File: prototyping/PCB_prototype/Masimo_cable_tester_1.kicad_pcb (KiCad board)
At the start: 2 copper layers, 70 x 80 mm, 30 parts, among them J1 Touchscreen HMI, J10 MCU Board Power, J16 Debug Connections, J17 Banana Jack, J2 Curiosity Nano AVR128DB48, J3 Conn_01x28_Socket, J4 Barrel Jack 9V, J5 MicroSD PinHeader, J6 SFML-110-02-L-D-A, J7 HMI Power Toggle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

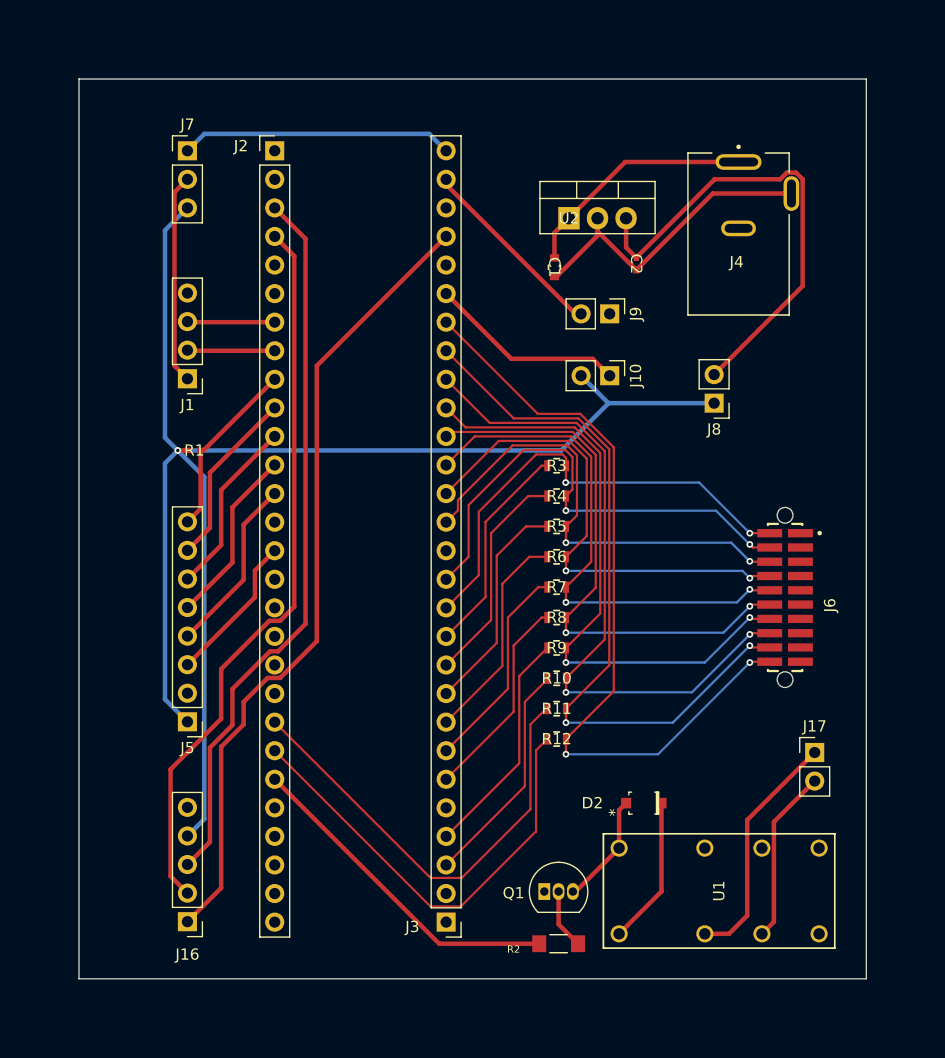
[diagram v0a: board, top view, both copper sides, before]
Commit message: Added ground plane.
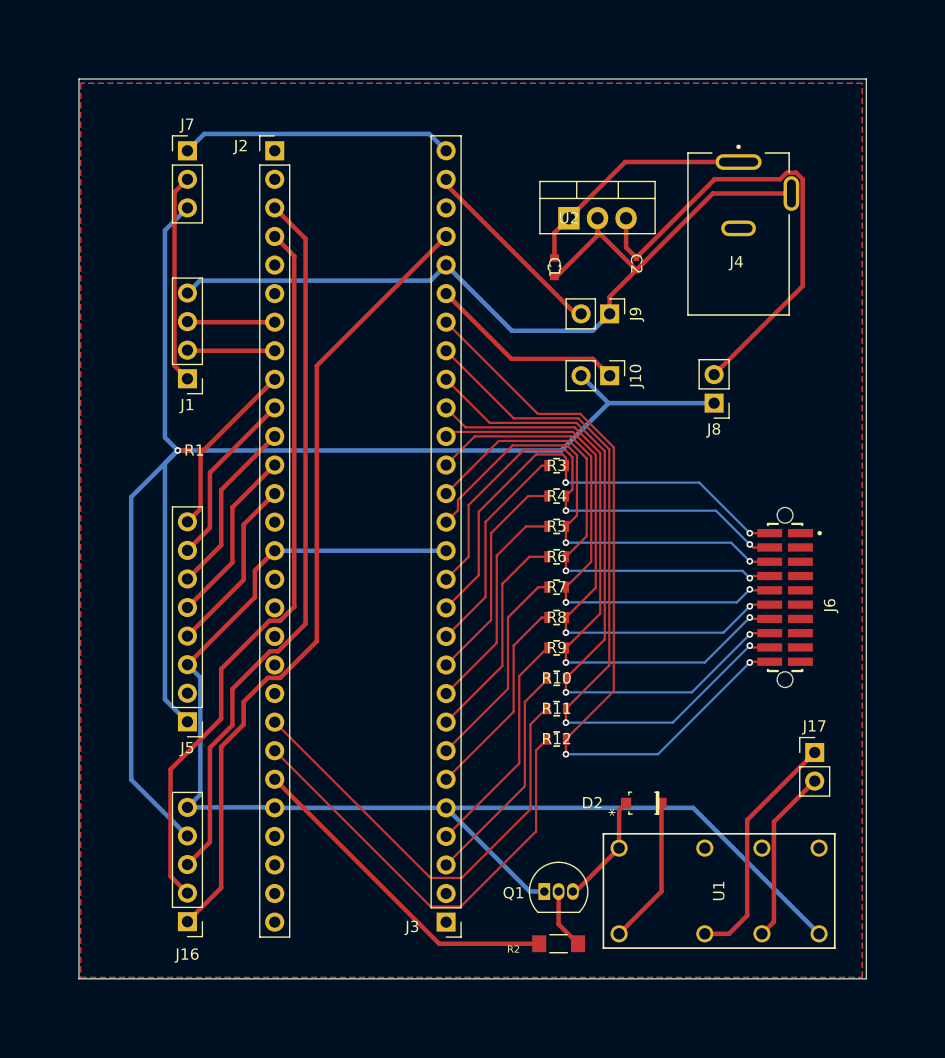
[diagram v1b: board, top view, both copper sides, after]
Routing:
- net GND: track 42.9 -> 190.9 mm
- net 5V: track 151.1 -> 153.3 mm
- added copper zone on B.Cu, net GND
- added copper zone on F.Cu, net GND
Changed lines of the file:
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@@
+	)
+	(segment
+		(start 127.54 70.975)
+		(end 129.9072 68.6078)
+		(width 0.4)
+		(layer "F.Cu")
+		(net 1)
 	)
 	(segment
@@
 		(width 0.4)
 		(layer "F.Cu")
+		(net 1)
+	)
+	(segment
+		(start 127.54 72.5)
+		(end 127.54 70.975)
+		(width 0.4)
+		(layer "F.Cu")
+		(net 1)
+	)
+	(segment
+		(start 118.84 74)
+		(end 126.04 74)
+		(width 0.4)
+		(layer "B.Cu")
+		(net 1)
+	)
+	(segment
+		(start 91.151 104.8411)
+		(end 91.151 115.229)
+		(width 0.4)
+		(layer "B.Cu")
+		(net 1)
+	)
+	(segment
+		(start 113 116.42)
+		(end 120.44 123.86)
+		(width 0.4)
+		(layer "B.Cu")
+		(net 1)
+	)
+	(segment
+		(start 113 68.16)
+		(end 111.611 69.549)
+		(width 0.4)
+		(layer "B.Cu")
+		(net 1)
+	)
+	(segment
+		(start 91.151 115.229)
+		(end 90 116.38)
+		(width 0.4)
+		(layer "B.Cu")
+		(net 1)
+	)
+	(segment
+		(start 134.96 116.42)
+		(end 146.16 127.62)
+		(width 0.4)
+		(layer "B.Cu")
+		(net 1)
+	)
+	(segment
+		(start 113 116.42)
+		(end 97.76 116.42)
+		(width 0.4)
+		(layer "B.Cu")
+		(net 1)
+	)
+	(segment
+		(start 113 93.56)
+		(end 97.76 93.56)
+		(width 0.4)
+		(layer "B.Cu")
+		(net 1)
+	)
+	(segment
+		(start 113 116.42)
+		(end 134.96 116.42)
+		(width 0.4)
+		(layer "B.Cu")
+		(net 1)
+	)
+	(segment
+		(start 90 103.6901)
+		(end 91.151 104.8411)
+		(width 0.4)
+		(layer "B.Cu")
+		(net 1)
+	)
+	(segment
+		(start 90 116.38)
+		(end 97.72 116.38)
+		(width 0.4)
+		(layer "B.Cu")
+		(net 1)
+	)
+	(segment
+		(start 111.611 69.549)
+		(end 91.1009 69.549)
+		(width 0.4)
+		(layer "B.Cu")
+		(net 1)
+	)
+	(segment
+		(start 97.72 116.38)
+		(end 97.76 116.42)
+		(width 0.2)
+		(layer "B.Cu")
+		(net 1)
+	)
+	(segment
+		(start 120.44 123.86)
+		(end 121.73 123.86)
+		(width 0.4)
+		(layer "B.Cu")
+		(net 1)
+	)
+	(segment
+		(start 126.04 74)
+		(end 127.54 72.5)
+		(width 0.4)
+		(layer "B.Cu")
+		(net 1)
+	)
+	(segment
+		(start 113 68.16)
+		(end 118.84 74)
+		(width 0.4)
+		(layer "B.Cu")
+		(net 1)
+	)
+	(segment
+		(start 91.1009 69.549)
+		(end 90 70.6499)
+		(width 0.4)
+		(layer "B.Cu")
 		(net 1)
 	)
@@
 	)
 	(segment
-		(start 91.5 87)
-		(end 91.5 117.42)
-		(width 0.4)
-		(layer "B.Cu")
-		(net 58)
-	)
-	(segment
 		(start 88 83.5)
 		(end 89.145 84.645)
@@
 	)
 	(segment
+		(start 85 113.92)
+		(end 90 118.92)
+		(width 0.4)
+		(layer "B.Cu")
+		(net 58)
+	)
+	(segment
 		(start 136.8278 80.44)
 		(end 127.44 80.44)
@@
 	)
 	(segment
+		(start 89.145 84.645)
+		(end 85 88.79)
+		(width 0.4)
+		(layer "B.Cu")
+		(net 58)
+	)
+	(segment
 		(start 123.235 84.645)
 		(end 127.44 80.44)
@@
 	)
 	(segment
-		(start 89.145 84.645)
-		(end 91.5 87)
-		(width 0.4)
-		(layer "B.Cu")
-		(net 58)
-	)
-	(segment
-		(start 91.5 117.42)
-		(end 90 118.92)
+		(start 85 88.79)
+		(end 85 113.92)
 		(width 0.4)
 		(layer "B.Cu")
@@
 		(net 75)
 	)
+	(zone
+		(net 1)
+		(net_name "GND")
+		(layers "F.Cu" "B.Cu")
+		(hatch edge 0.5)
+		(connect_pads
+			(clearance 0.5)
+		)
+		(min_thickness 0.25)
+		(filled_areas_thickness no)
+		(fill
+			(thermal_gap 0.5)
+			(thermal_bridge_width 0.5)
+		)
+		(polygon
+			(pts
+				(xy 80.5 52) (xy 80.5 131.5) (xy 150 131.5) (xy 150 52)
+			)
+		)
+	)
 	(embedded_fonts no)

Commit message: Prototype PCB update
extended the board to add screw mount holes
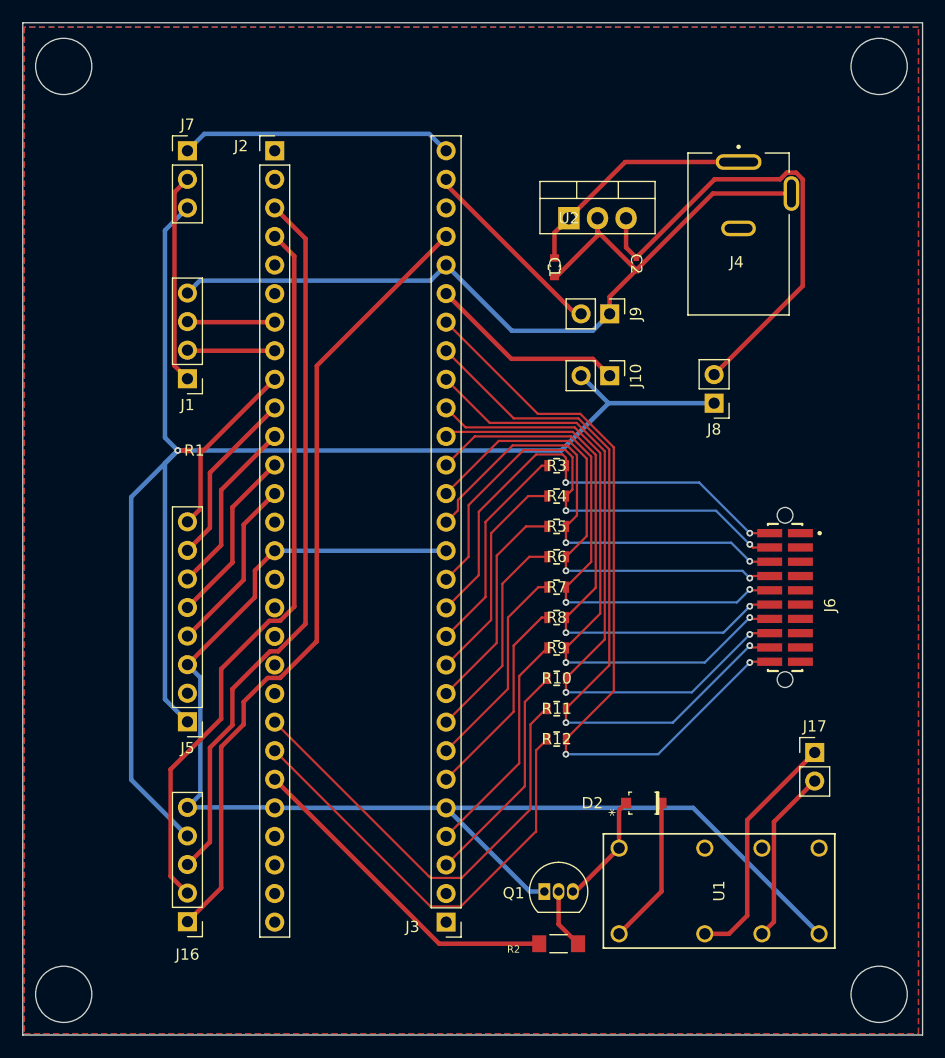
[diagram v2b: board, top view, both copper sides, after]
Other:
- board size 70 x 80 mm -> 80 x 90 mm

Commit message: Changed spacing.
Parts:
- moved J4 9.30 mm to (148.3, 64.9)
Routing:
- net Net-(J8-Pin_2): track 42.7 -> 57.2 mm
- net GND: track 190.9 -> 200.2 mm
- net 9V: track 21.2 -> 30.5 mm
